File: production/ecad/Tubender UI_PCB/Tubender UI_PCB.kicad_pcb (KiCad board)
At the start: 4 copper layers, 72.5 x 87.5 mm, 18 parts, among them IC3 SN74LVC1G29DCTR, J1 640387-5, J2 1-640387-0, J3 104031-0811, J4 640387-5, U5 74HC595, U6 PEC11R-4215K-S0024

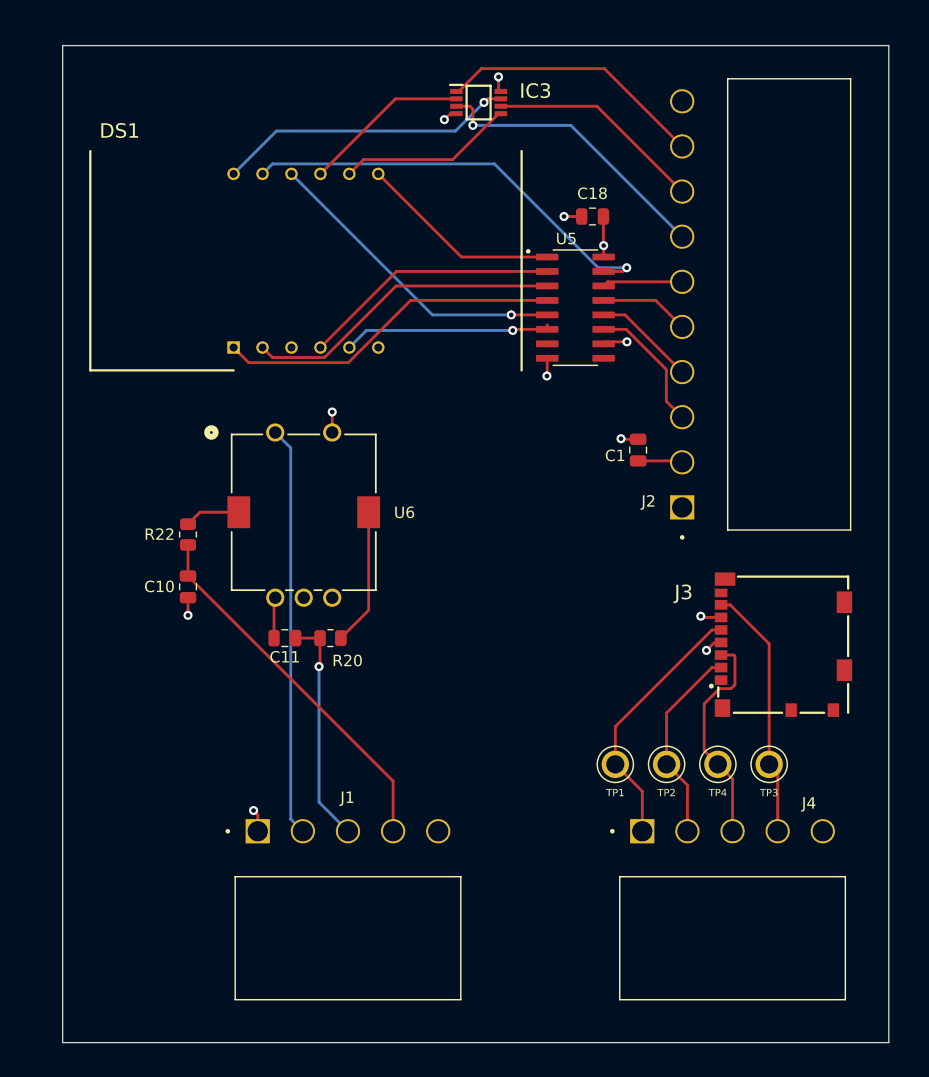
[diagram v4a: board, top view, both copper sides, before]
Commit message: Fixed DRC issues with UI board and added mounting holes
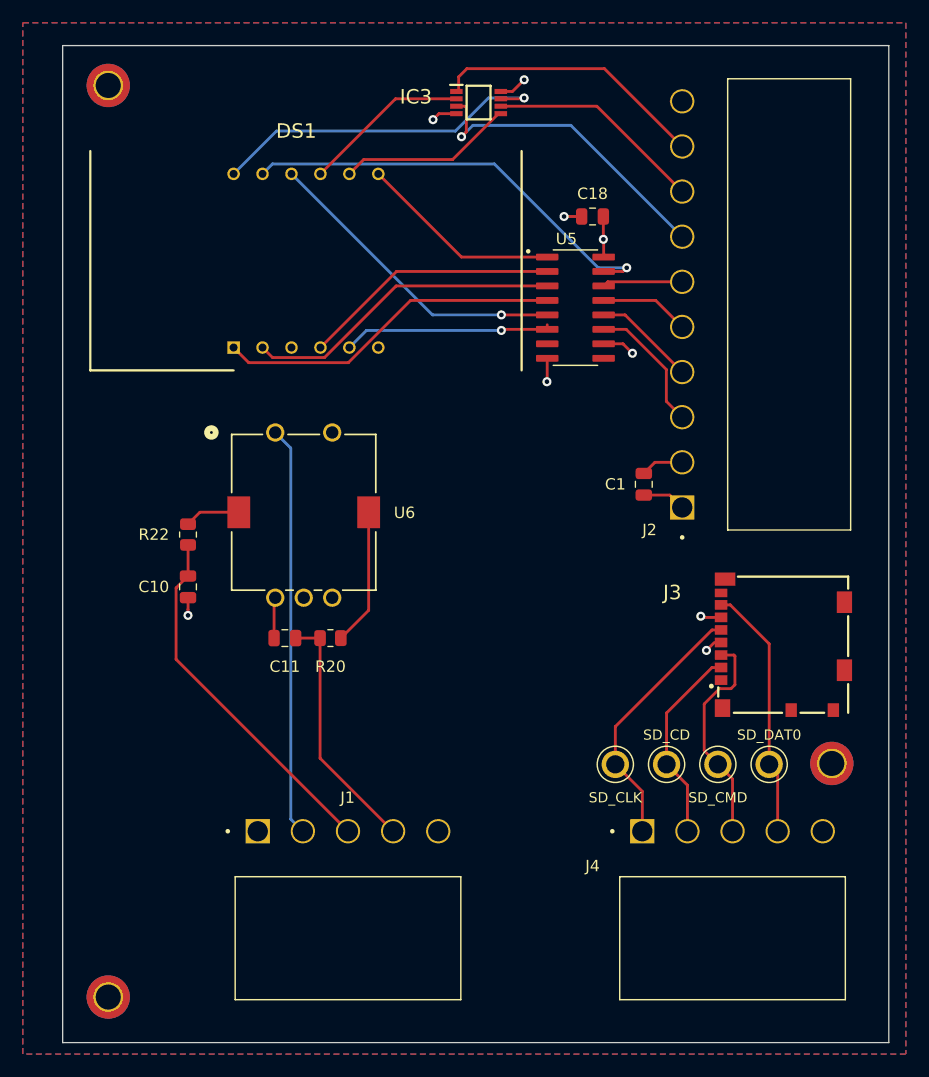
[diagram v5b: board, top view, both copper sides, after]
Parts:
- added REF**: MountingHole_2.2mm_M2_DIN965_Pad_TopBottom, MountingHole:MountingHole_2.2mm_M2_DIN965_Pad_TopBottom, F.Cu at (97.5, 88.5)
- added REF**: MountingHole_2.2mm_M2_DIN965_Pad_TopBottom, MountingHole:MountingHole_2.2mm_M2_DIN965_Pad_TopBottom, F.Cu at (161.0, 148.0)
- added REF**: MountingHole_2.2mm_M2_DIN965_Pad_TopBottom, MountingHole:MountingHole_2.2mm_M2_DIN965_Pad_TopBottom, F.Cu at (97.5, 168.5)
- moved C1 3.04 mm to (144.5, 123.5), turned to -90 degrees
- renumbered TP2 to SD_CD, TP1 to SD_CLK, TP4 to SD_CMD, TP3 to SD_DAT0
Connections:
- J1 pad 3: DIAL_CHANNEL_B -> DIAL_CHANNEL_A
- J1 pad 4: DIAL_CHANNEL_A -> DIAL_CHANNEL_B
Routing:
- net Net-(DS1-COMMON_CATHODE_DIG1): track 26.4 -> 30.3 mm
- net GND: track 13.1 -> 16.9 mm, vias 6 -> 5
- net +5V: track 9.67 -> 7.25 mm, vias 4 -> 2
- net 7-SEG_A0: track 25.2 -> 27.3 mm
- net DIAL_CHANNEL_B: track 20.2 -> 21.7 mm, vias 1 -> 0
- net +3V3: track 7.03 -> 7.80 mm
- net DIAL_CHANNEL_A: track 32.6 -> 31.8 mm
- net 7-SEG_Gb: track 23.3 -> 24.0 mm
- added copper zone on B.Cu, net GND
- added copper zone on F.Cu, net GND
